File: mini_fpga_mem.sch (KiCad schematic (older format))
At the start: 1 part

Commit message: Power supply section complete! (hopefully)
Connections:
- net +1.25V: now reaches U?.C1 (IO_L83N_VREF_3)
- net +1.25V: now also U?.L3 (IO_L1N_VREF_3)
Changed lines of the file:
@@
 Sheet 3 6
 Title ""
-Date "19 jul 2014"
+Date "24 jul 2014"
 Rev ""
 Comp ""
@@
 	1    0    0    -1
 $EndComp
+$Comp
+L +1.25V #PWR?
+U 1 1 53CC7509
+P 6100 5100
+F 0 "#PWR?" H 6100 5050 20  0001 C CNN
+F 1 "+1.25V" H 6100 5200 30  0000 C CNN
+F 2 "~" H 6100 5100 60  0000 C CNN
+F 3 "~" H 6100 5100 60  0000 C CNN
+	1    6100 5100
+	1    0    0    -1
+$EndComp
+Wire Wire Line
+	5350 5150 6100 5150
+Wire Wire Line
+	6100 5150 6100 5100
+$Comp
+L +1.25V #PWR?
+U 1 1 53CC7523
+P 1450 2300
+F 0 "#PWR?" H 1450 2250 20  0001 C CNN
+F 1 "+1.25V" H 1450 2400 30  0000 C CNN
+F 2 "~" H 1450 2300 60  0000 C CNN
+F 3 "~" H 1450 2300 60  0000 C CNN
+	1    1450 2300
+	1    0    0    -1
+$EndComp
+Wire Wire Line
+	1950 2350 1450 2350
+Wire Wire Line
+	1450 2350 1450 2300
 $EndSCHEMATC

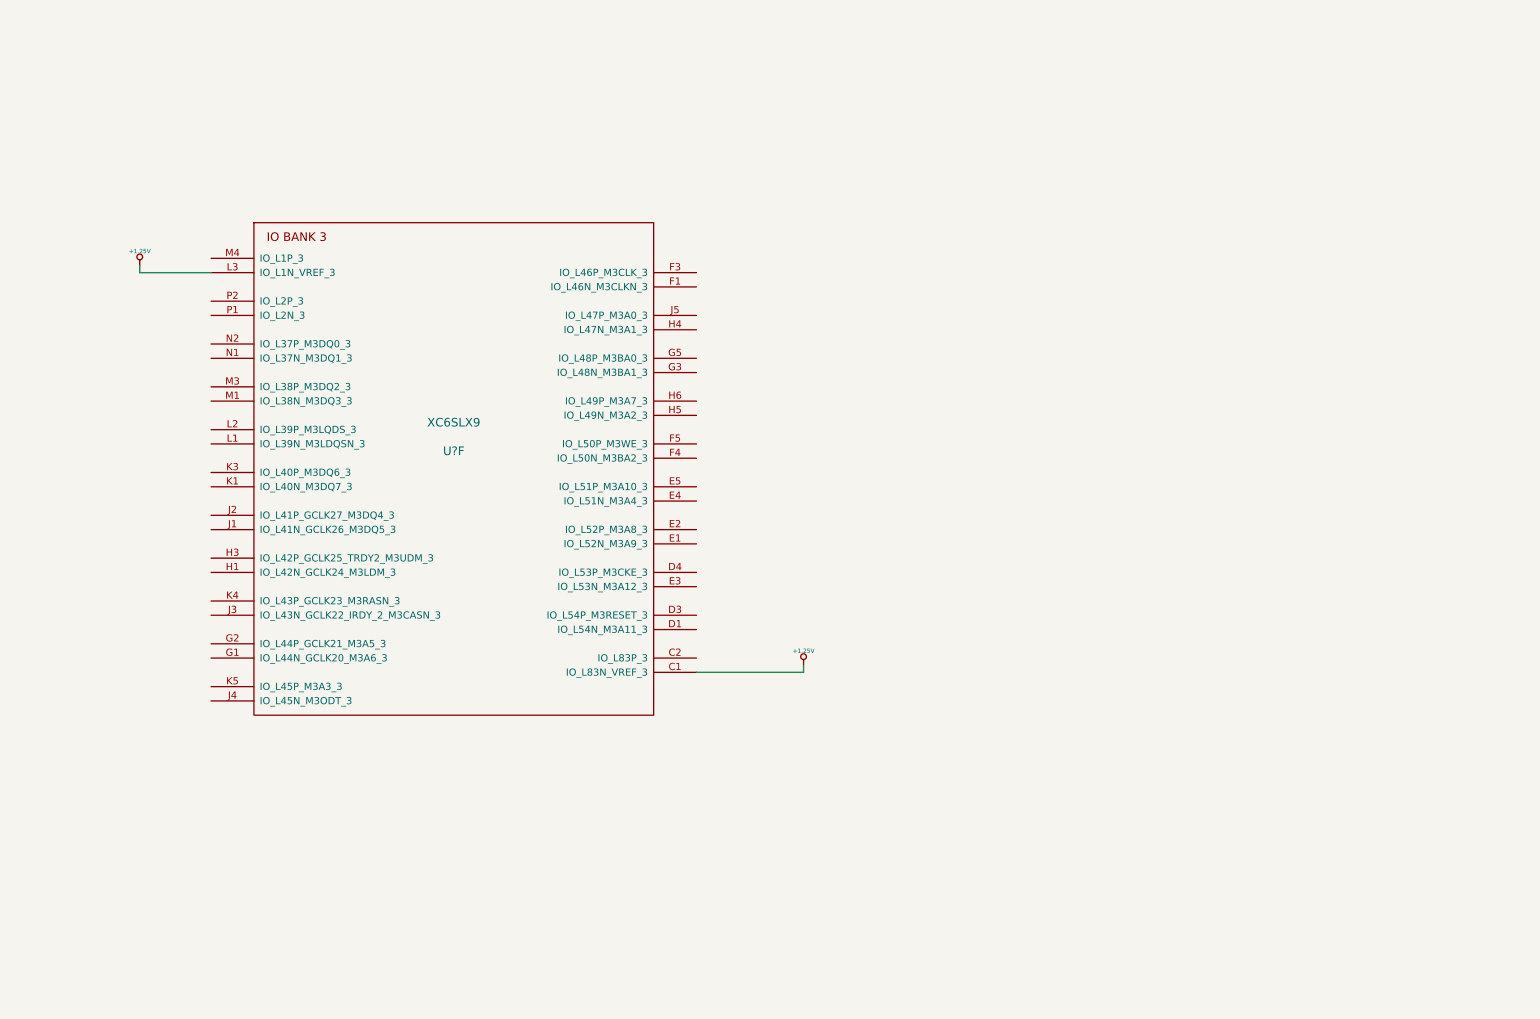
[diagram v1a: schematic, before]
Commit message: Memory power design finished.
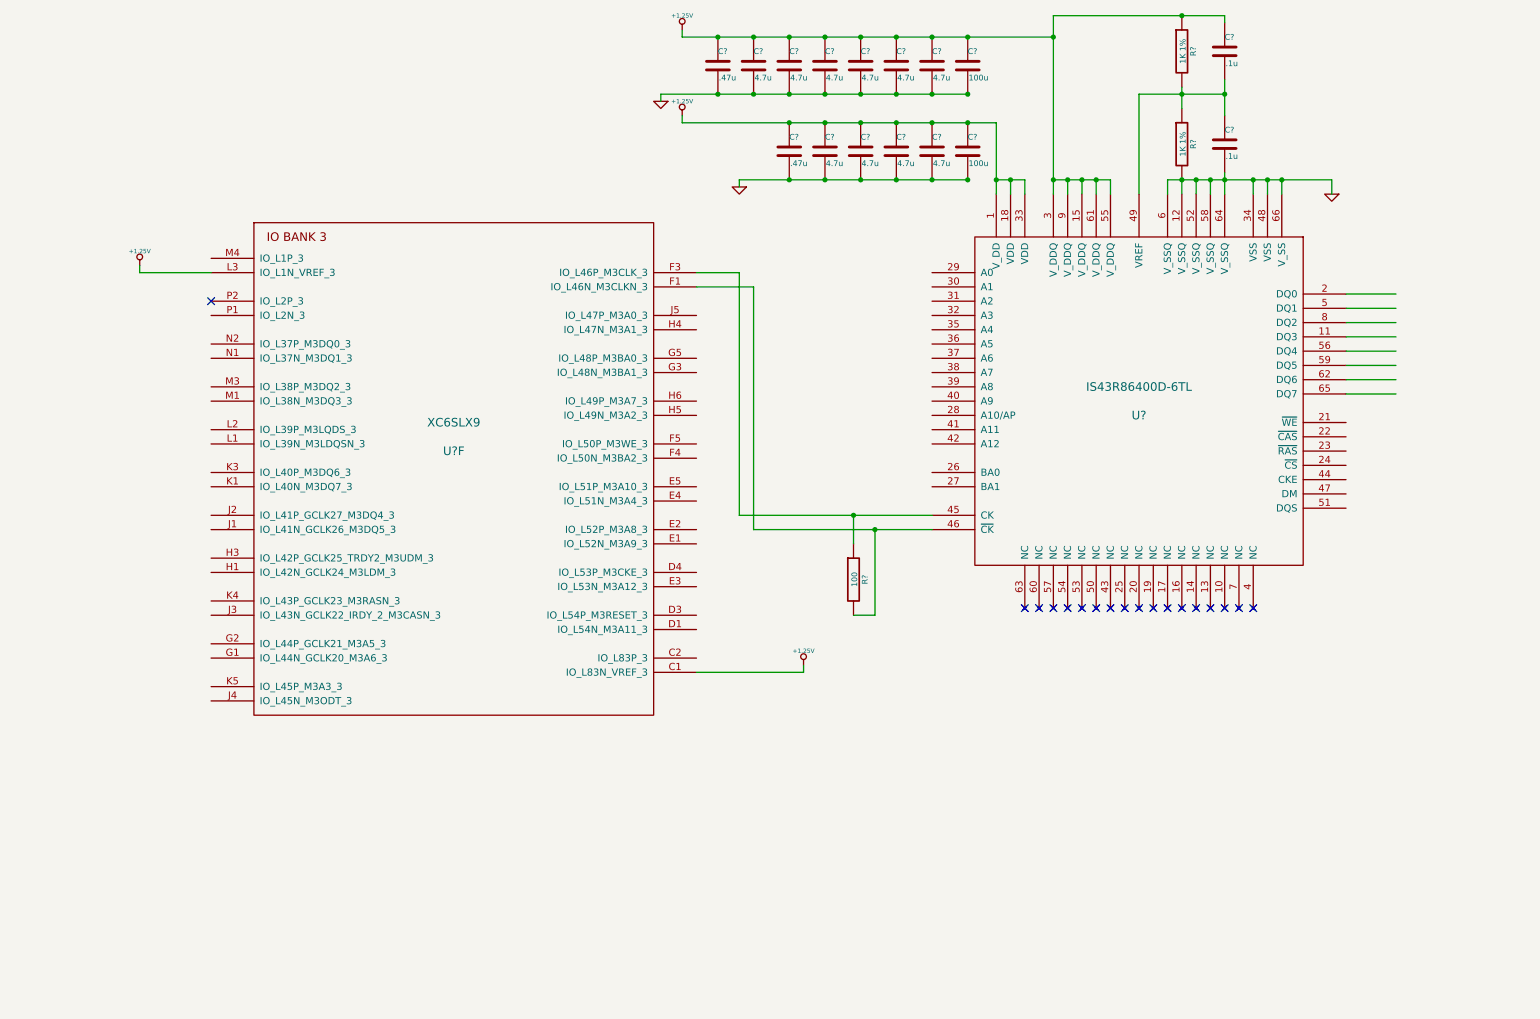
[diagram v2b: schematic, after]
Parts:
- added C? (x2): .1u, ~, symbol C
- added C? (x10): 4.7u, ~, symbol C
- added C? (x2): .47u, ~, symbol C
- added C? (x2): 100u, ~, symbol C
- added R? (x2): 1K 1%, ~, symbol R
- added R?: 100, ~, symbol R
- added U?: IS43R86400D-6TL, symbol IS43R86400D-6TL
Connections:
- net labels added: GND
- wire segments 4 -> 55
- no-connect marks 0 -> 18

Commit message: Finish memory layout (hopefully!)
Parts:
- added C? (x2): .1u, ~, symbol C
- added R? (x29): 50, ~, symbol R
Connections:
- net labels added: RAM_A, RAM_A0, RAM_A1, RAM_A10, RAM_A11, RAM_A12, RAM_A2, RAM_A3, RAM_A4, RAM_A5, RAM_A6, RAM_A7, RAM_A8, RAM_A9, RAM_BA0, RAM_BA1, RAM_CKE, RAM_Control, RAM_DM, RAM_DQ, RAM_DQ0, RAM_DQ1, RAM_DQ2, RAM_DQ3, RAM_DQ4, RAM_DQ5, RAM_DQ6, RAM_DQ7, RAM_DQS, RAM_~CAS~, RAM_~RAS~, RAM_~WE~, Vref
- wire segments 55 -> 172
- no-connect marks 18 -> 25
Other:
- moved on the sheet: R?, U?F

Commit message: First checkover of schematic complete, should be working.
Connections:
- net RAM_~CAS~: now also R?.2; no longer R?.2
- net RAM_~RAS~: now also R?.2; no longer R?.2
- no-connect marks 25 -> 26
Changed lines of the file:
@@
 Sheet 3 6
 Title ""
-Date "26 jul 2014"
+Date "28 jul 2014"
 Rev ""
 Comp ""
@@
 Entry Wire Line
 	550  6300 650  6400
+Text Label 650  6500 0    60   ~ 0
+RAM_~CAS~
 Text Label 650  6400 0    60   ~ 0
-RAM_~CAS~
-Text Label 650  6500 0    60   ~ 0
 RAM_~RAS~
 Wire Wire Line
@@
 	2000 3950 2000 4050
 Connection ~ 2000 4050
+NoConn ~ 5500 6450
 $EndSCHEMATC

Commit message: Annotated!
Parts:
- gave numbers to parts that had none: 52

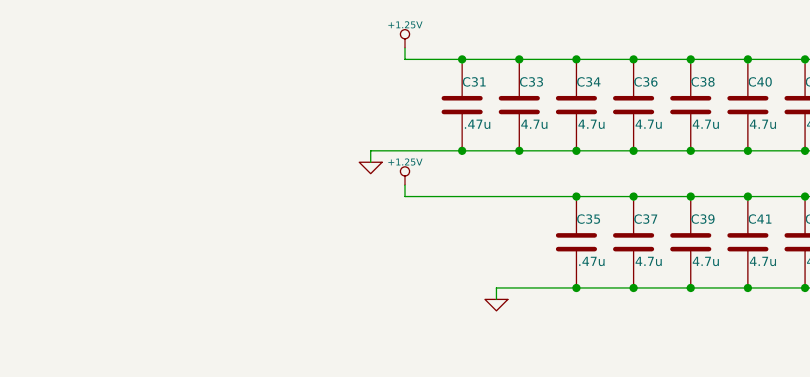
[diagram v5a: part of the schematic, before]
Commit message: Some small errors corrected
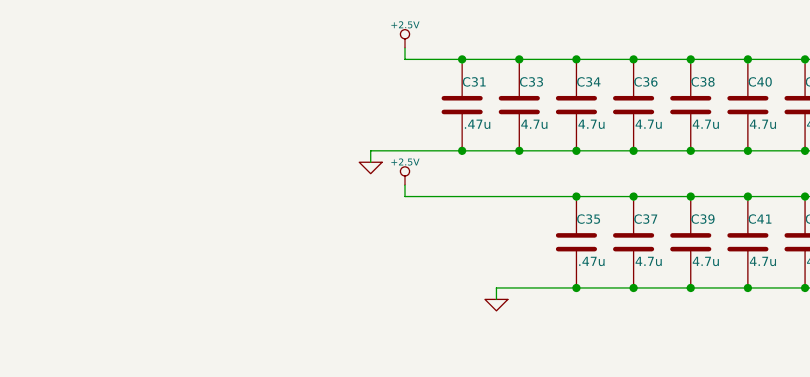
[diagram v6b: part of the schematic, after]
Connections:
- net +1.25V renamed +2.5V
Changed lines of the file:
@@
 $EndComp
 $Comp
-L GND #PWR35
+L GND #PWR029
 U 1 1 53D1BABF
 P 9800 1800
-F 0 "#PWR35" H 9800 1800 30  0001 C CNN
+F 0 "#PWR029" H 9800 1800 30  0001 C CNN
 F 1 "GND" H 9800 1730 30  0001 C CNN
 F 2 "" H 9800 1800 60  0000 C CNN
@@
 	1    0    0    -1
 $EndComp
-$Comp
-L +1.25V #PWR31
-U 1 1 53D2BD24
-P 5250 650
-F 0 "#PWR31" H 5250 600 20  0001 C CNN
-F 1 "+1.25V" H 5250 750 30  0000 C CNN
-F 2 "~" H 5250 650 60  0000 C CNN
-F 3 "~" H 5250 650 60  0000 C CNN
-	1    5250 650
-	1    0    0    -1
-$EndComp
-$Comp
-L +1.25V #PWR32
-U 1 1 53D2BD71
-P 5250 1250
-F 0 "#PWR32" H 5250 1200 20  0001 C CNN
-F 1 "+1.25V" H 5250 1350 30  0000 C CNN
-F 2 "~" H 5250 1250 60  0000 C CNN
-F 3 "~" H 5250 1250 60  0000 C CNN
-	1    5250 1250
-	1    0    0    -1
-$EndComp
 Wire Wire Line
 	7850 550  7850 1800
@@
 Connection ~ 9050 1100
 $Comp
-L GND #PWR30
+L GND #PWR032
 U 1 1 53D2BFD1
 P 5100 1150
-F 0 "#PWR30" H 5100 1150 30  0001 C CNN
+F 0 "#PWR032" H 5100 1150 30  0001 C CNN
 F 1 "GND" H 5100 1080 30  0001 C CNN
 F 2 "" H 5100 1150 60  0000 C CNN
@@
 $EndComp
 $Comp
-L GND #PWR34
+L GND #PWR033
 U 1 1 53D2C31E
 P 5650 1750
-F 0 "#PWR34" H 5650 1750 30  0001 C CNN
+F 0 "#PWR033" H 5650 1750 30  0001 C CNN
 F 1 "GND" H 5650 1680 30  0001 C CNN
 F 2 "" H 5650 1750 60  0000 C CNN
@@
 RAM_DM
 $Comp
-L GND #PWR36
+L GND #PWR034
 U 1 1 53D44EBA
 P 10700 3800
-F 0 "#PWR36" H 10700 3800 30  0001 C CNN
+F 0 "#PWR034" H 10700 3800 30  0001 C CNN
 F 1 "GND" H 10700 3730 30  0001 C CNN
 F 2 "" H 10700 3800 60  0000 C CNN
@@
 	5600 7350 5600 7450
 $Comp
-L GND #PWR33
+L GND #PWR035
 U 1 1 53D4560F
 P 5600 7450
-F 0 "#PWR33" H 5600 7450 30  0001 C CNN
+F 0 "#PWR035" H 5600 7450 30  0001 C CNN
 F 1 "GND" H 5600 7380 30  0001 C CNN
 F 2 "" H 5600 7450 60  0000 C CNN
@@
 $EndComp
 $Comp
-L GND #PWR29
+L GND #PWR036
 U 1 1 53D4561C
 P 1800 3550
-F 0 "#PWR29" H 1800 3550 30  0001 C CNN
+F 0 "#PWR036" H 1800 3550 30  0001 C CNN
 F 1 "GND" H 1800 3480 30  0001 C CNN
 F 2 "" H 1800 3550 60  0000 C CNN
@@
 Connection ~ 2000 4050
 NoConn ~ 5500 6450
+$Comp
+L +2.5V #PWR?
+U 1 1 53D5E29D
+P 5250 650
+F 0 "#PWR?" H 5250 600 20  0001 C CNN
+F 1 "+2.5V" H 5250 750 30  0000 C CNN
+F 2 "" H 5250 650 60  0000 C CNN
+F 3 "" H 5250 650 60  0000 C CNN
+	1    5250 650
+	1    0    0    -1
+$EndComp
+$Comp
+L +2.5V #PWR?
+U 1 1 53D5E2AA
+P 5250 1250
+F 0 "#PWR?" H 5250 1200 20  0001 C CNN
+F 1 "+2.5V" H 5250 1350 30  0000 C CNN
+F 2 "" H 5250 1250 60  0000 C CNN
+F 3 "" H 5250 1250 60  0000 C CNN
+	1    5250 1250
+	1    0    0    -1
+$EndComp
 $EndSCHEMATC
